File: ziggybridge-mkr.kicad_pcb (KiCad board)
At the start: 4 copper layers, 55.2 x 45.7 mm, 14 parts, among them J1 Conn_01x14, J10 Conn_01x06, J11 Conn_01x08, J12 Conn_01x08, J2 Conn_01x14, J5 Conn_01x03, J6 Conn_01x04, J7 Conn_01x06, J8 Conn_01x06, J9 Conn_01x06

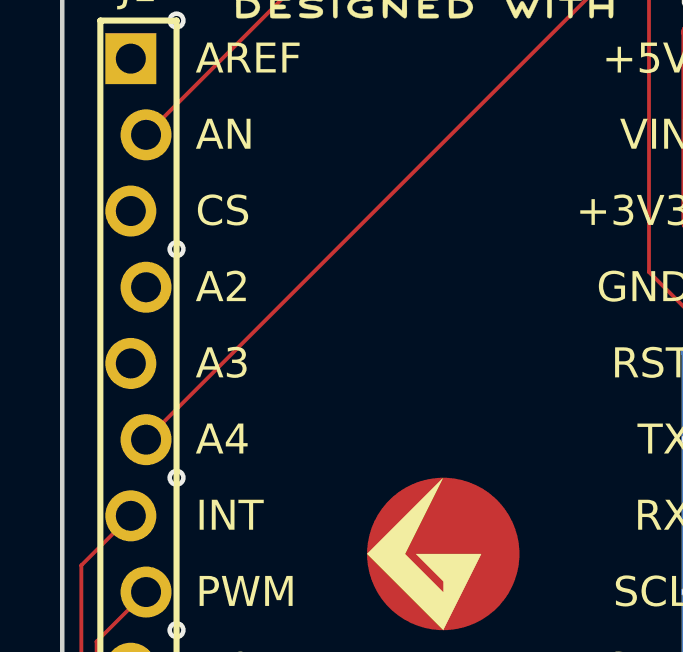
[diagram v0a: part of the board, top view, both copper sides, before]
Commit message: fixed labels on MKR socket
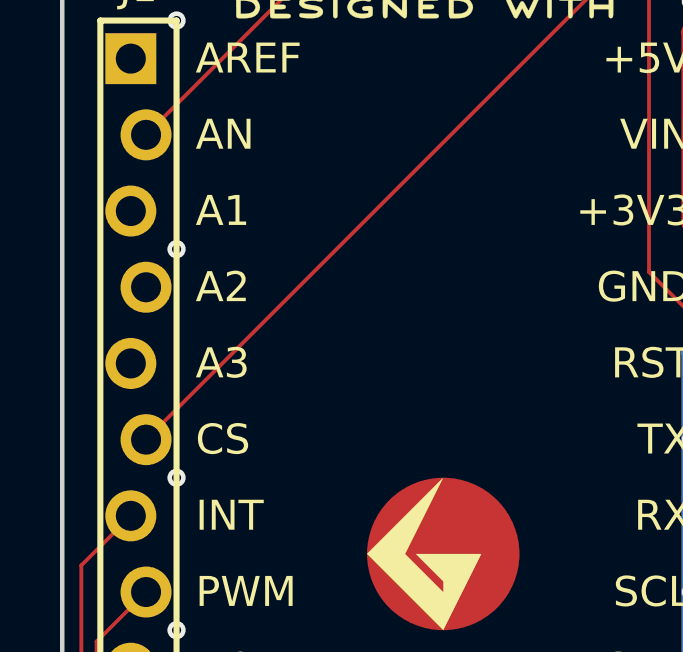
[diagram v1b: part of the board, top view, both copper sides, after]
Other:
- board text added: "A1"
- board text removed: "A4"
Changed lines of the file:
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@@
 		)
 	)
-	(gr_text "A4"
+	(gr_text "CS"
 		(at 131.445 110.49 0)
 		(layer "F.SilkS")
@@
 		)
 	)
-	(gr_text "CS"
+	(gr_text "A1"
 		(at 131.445 102.87 0)
 		(layer "F.SilkS")
@@
 		)
 	)
-	(gr_text "CS"
+	(gr_text "A1"
 		(at 130.81 102.87 0)
 		(layer "B.SilkS")
@@
 		)
 	)
-	(gr_text "A4"
+	(gr_text "CS"
 		(at 130.81 110.49 0)
 		(layer "B.SilkS")

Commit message: changed to 2 layers
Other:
- copper layers 4 -> 2
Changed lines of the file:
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@@
 	(layers
 		(0 "F.Cu" signal "Top")
-		(4 "In1.Cu" signal "LFSignals")
-		(6 "In2.Cu" signal "POWER")
 		(2 "B.Cu" signal "Bottom")
 		(9 "F.Adhes" user "F.Adhesive")
@@
 	)
 	(setup
+		(stackup
+			(layer "F.SilkS"
+				(type "Top Silk Screen")
+			)
+			(layer "F.Paste"
+				(type "Top Solder Paste")
+			)
+			(layer "F.Mask"
+				(type "Top Solder Mask")
+				(thickness 0.01)
+			)
+			(layer "F.Cu"
+				(type "copper")
+				(thickness 0.035)
+			)
+			(layer "dielectric 1"
+				(type "core")
+				(thickness 1.51)
+				(material "FR4")
+				(epsilon_r 4.5)
+				(loss_tangent 0.02)
+			)
+			(layer "B.Cu"
+				(type "copper")
+				(thickness 0.035)
+			)
+			(layer "B.Mask"
+				(type "Bottom Solder Mask")
+				(thickness 0.01)
+			)
+			(layer "B.Paste"
+				(type "Bottom Solder Paste")
+			)
+			(layer "B.SilkS"
+				(type "Bottom Silk Screen")
+			)
+			(copper_finish "None")
+			(dielectric_constraints no)
+		)
 		(pad_to_mask_clearance 0.1016)
 		(solder_mask_min_width 0.127)

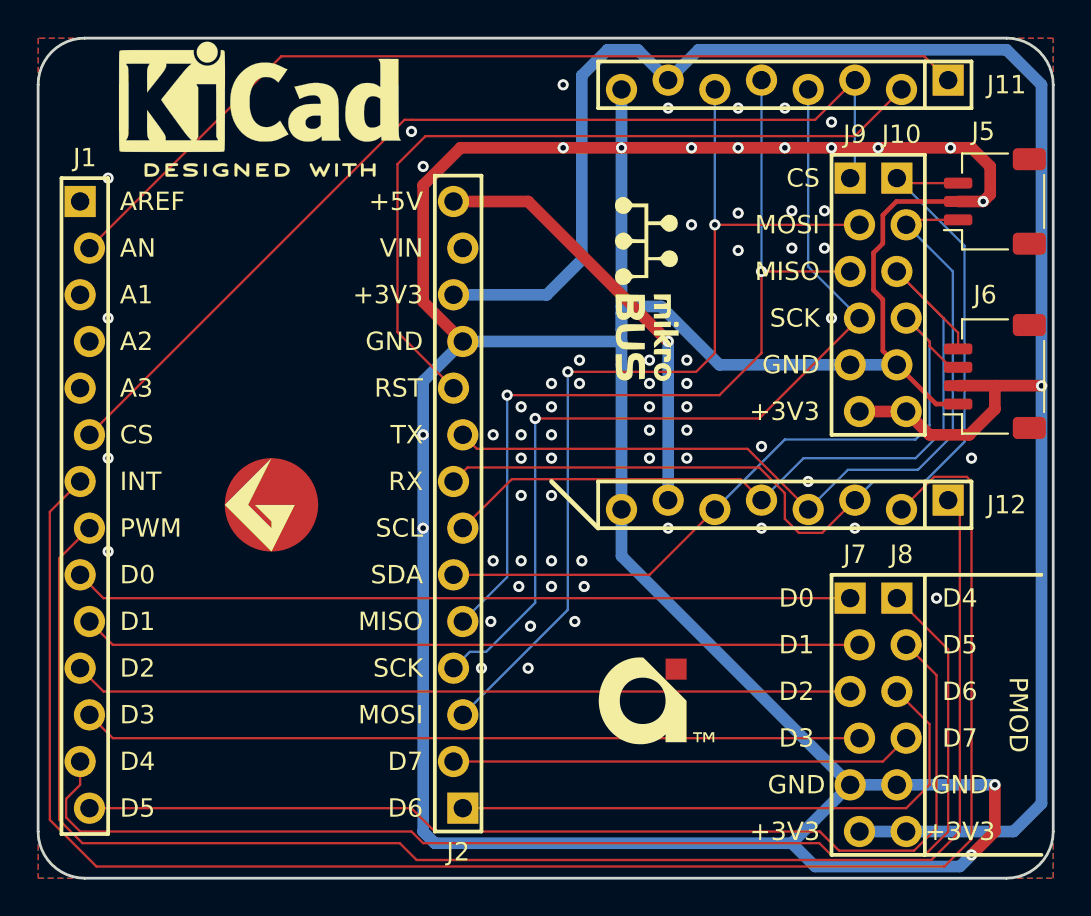
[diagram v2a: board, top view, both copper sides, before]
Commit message: cleaned up design, removed soldermask adjustments and wide ground traces that were defeating thermal releifs
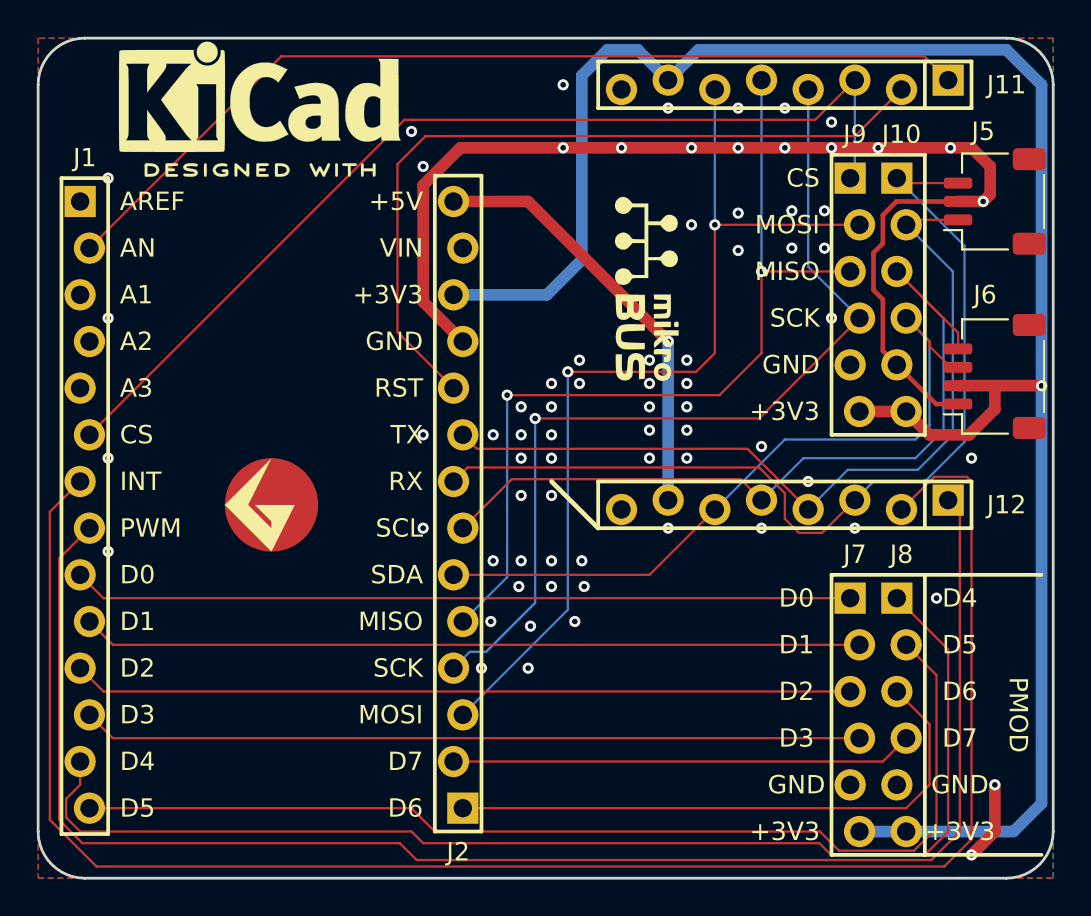
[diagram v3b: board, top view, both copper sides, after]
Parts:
- removed the G*** at (160.7, 125.0)
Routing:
- net GND: track 206.8 -> 66.8 mm
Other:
- rule pad_to_mask_clearance: 0.1016 -> 0
